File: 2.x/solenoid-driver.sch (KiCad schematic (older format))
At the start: 69 parts, among them P3 CONN_8X2, Q1 BC846, Q10 BC846, Q11 BC846, Q12 BC846, Q2 BC846, Q3 BC846, Q4 BC846, Q5 DMN6040SSD, Q6 DMN6040SSD, Q7 DMN6040SSD, Q8 DMN6040SSD, Q9 BC846

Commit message: Cleaning up schematic Updating solenoid driver to use 12V for MOSFET gates instead of Vsol so we never exceed Vgs_max
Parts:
- R11, R13, R15, R33, R35, R37, R39, R9: value 18K -> 1K
- R21, R22, R23, R24, R25, R26, R27, R28: value 27K -> 4.7K
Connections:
- net labels added: SOL_12V
- wire segments 244 -> 245
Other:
- moved on the sheet: D1, D2, D3, D4, D5, D6, D7, D8, Q1, Q10, Q11, Q12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

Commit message: Started layout on 2.0
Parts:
- removed P3: CONN_8X2, symbol CONN_8X2
- added D39, D40, D41, D42, D43, D44, D45, D46: S1M, Diodes_SMD:Diode-SMA_Standard, symbol DIODE
- added P3: SOLENOID-CONNECTOR, PinballParts:SOLENOID-CONNECTOR-V, symbol SOLENOID-CONNECTOR
- D1, D8: footprint ~ -> LEDs:LED-0603
- D2: renamed from D5; footprint ~ -> LEDs:LED-0603
- D3: renamed from D2; footprint ~ -> LEDs:LED-0603
- D4: renamed from D6; footprint ~ -> LEDs:LED-0603
- D5: renamed from D3; footprint ~ -> LEDs:LED-0603
- D6: renamed from D7; footprint ~ -> LEDs:LED-0603
- D7: renamed from D4; footprint ~ -> LEDs:LED-0603
- Q1, Q12: footprint SOT-23 -> Housings_SOT-23_SOT-143_TSOT-6:SOT-23
- Q10: renamed from Q8; footprint SO8 -> Housings_SOIC:SOIC-8_3.9x4.9mm_Pitch1.27mm
- Q11: renamed from Q4; footprint SOT-23 -> Housings_SOT-23_SOT-143_TSOT-6:SOT-23
- Q2: renamed from Q9; footprint SOT-23 -> Housings_SOT-23_SOT-143_TSOT-6:SOT-23
- Q3: renamed from Q5; footprint SO8 -> Housings_SOIC:SOIC-8_3.9x4.9mm_Pitch1.27mm
- Q4: renamed from Q7; footprint SO8 -> Housings_SOIC:SOIC-8_3.9x4.9mm_Pitch1.27mm
- Q5: renamed from Q2; footprint SOT-23 -> Housings_SOT-23_SOT-143_TSOT-6:SOT-23
- Q6: renamed from Q10; footprint SOT-23 -> Housings_SOT-23_SOT-143_TSOT-6:SOT-23
- Q7: renamed from Q3; footprint SOT-23 -> Housings_SOT-23_SOT-143_TSOT-6:SOT-23
- Q8: renamed from Q11; footprint SOT-23 -> Housings_SOT-23_SOT-143_TSOT-6:SOT-23
- Q9: renamed from Q6; footprint SO8 -> Housings_SOIC:SOIC-8_3.9x4.9mm_Pitch1.27mm
- R1: renamed from R5; footprint ~ -> Resistors_SMD:R_0603
- R10: renamed from R45; footprint ~ -> Resistors_SMD:R_0603
- R11: renamed from R17; footprint ~ -> Resistors_SMD:R_0603
- R12: renamed from R29; footprint ~ -> Resistors_SMD:R_0603
- R13: renamed from R6; footprint ~ -> Resistors_SMD:R_0603
- R14: renamed from R11; footprint ~ -> Resistors_SMD:R_0603
- R15: renamed from R22; value 4.7K -> 2.7K; footprint ~ -> Resistors_SMD:R_0603
- R16: renamed from R26; value 4.7K -> 2.7K; footprint ~ -> Resistors_SMD:R_0603
- R17: renamed from R35; footprint ~ -> Resistors_SMD:R_0603
- R18: renamed from R42; footprint ~ -> Resistors_SMD:R_0603
- R19: renamed from R2; footprint ~ -> Resistors_SMD:R_0603
- R2: renamed from R9; footprint ~ -> Resistors_SMD:R_0603
- R20: renamed from R12; footprint ~ -> Resistors_SMD:R_0603
- R21: renamed from R36; footprint ~ -> Resistors_SMD:R_0603
- R22: renamed from R46; footprint ~ -> Resistors_SMD:R_0603
- R23: renamed from R18; footprint ~ -> Resistors_SMD:R_0603
- R24: renamed from R30; footprint ~ -> Resistors_SMD:R_0603
- R25: renamed from R7; footprint ~ -> Resistors_SMD:R_0603
- R26: renamed from R13; footprint ~ -> Resistors_SMD:R_0603
- R27: renamed from R23; value 4.7K -> 2.7K; footprint ~ -> Resistors_SMD:R_0603
- R28: renamed from R27; value 4.7K -> 2.7K; footprint ~ -> Resistors_SMD:R_0603
- R29: renamed from R37; footprint ~ -> Resistors_SMD:R_0603
- R3: renamed from R21; value 4.7K -> 2.7K; footprint ~ -> Resistors_SMD:R_0603
- R30: renamed from R43; footprint ~ -> Resistors_SMD:R_0603
- R31: renamed from R3; footprint ~ -> Resistors_SMD:R_0603
- R32: renamed from R14; footprint ~ -> Resistors_SMD:R_0603
- R33: renamed from R38; footprint ~ -> Resistors_SMD:R_0603
- R34: renamed from R47; footprint ~ -> Resistors_SMD:R_0603
- R35: renamed from R19; footprint ~ -> Resistors_SMD:R_0603
- R36: renamed from R31; footprint ~ -> Resistors_SMD:R_0603
- R37: renamed from R8; footprint ~ -> Resistors_SMD:R_0603
- R38: renamed from R15; footprint ~ -> Resistors_SMD:R_0603
- R39: renamed from R24; value 4.7K -> 2.7K; footprint ~ -> Resistors_SMD:R_0603
- R4: renamed from R25; value 4.7K -> 2.7K; footprint ~ -> Resistors_SMD:R_0603
- R40: renamed from R28; value 4.7K -> 2.7K; footprint ~ -> Resistors_SMD:R_0603
- R41: renamed from R39; footprint ~ -> Resistors_SMD:R_0603
- R42: renamed from R44; footprint ~ -> Resistors_SMD:R_0603
- R43: renamed from R4; footprint ~ -> Resistors_SMD:R_0603
- R44: renamed from R16; footprint ~ -> Resistors_SMD:R_0603
- R45: renamed from R40; footprint ~ -> Resistors_SMD:R_0603
- R46: renamed from R48; footprint ~ -> Resistors_SMD:R_0603
- R47: renamed from R20; footprint ~ -> Resistors_SMD:R_0603
- R48: renamed from R32; footprint ~ -> Resistors_SMD:R_0603
- R5: renamed from R33; footprint ~ -> Resistors_SMD:R_0603
- R6: renamed from R41; footprint ~ -> Resistors_SMD:R_0603
- R7: renamed from R1; footprint ~ -> Resistors_SMD:R_0603
- R8: renamed from R10; footprint ~ -> Resistors_SMD:R_0603
- R9: renamed from R34; footprint ~ -> Resistors_SMD:R_0603
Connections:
- wire segments 245 -> 271
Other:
- moved on the sheet: D1, D2, D3, D4, D5, D6, D7, D8, Q1, Q10A, Q10B, Q11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

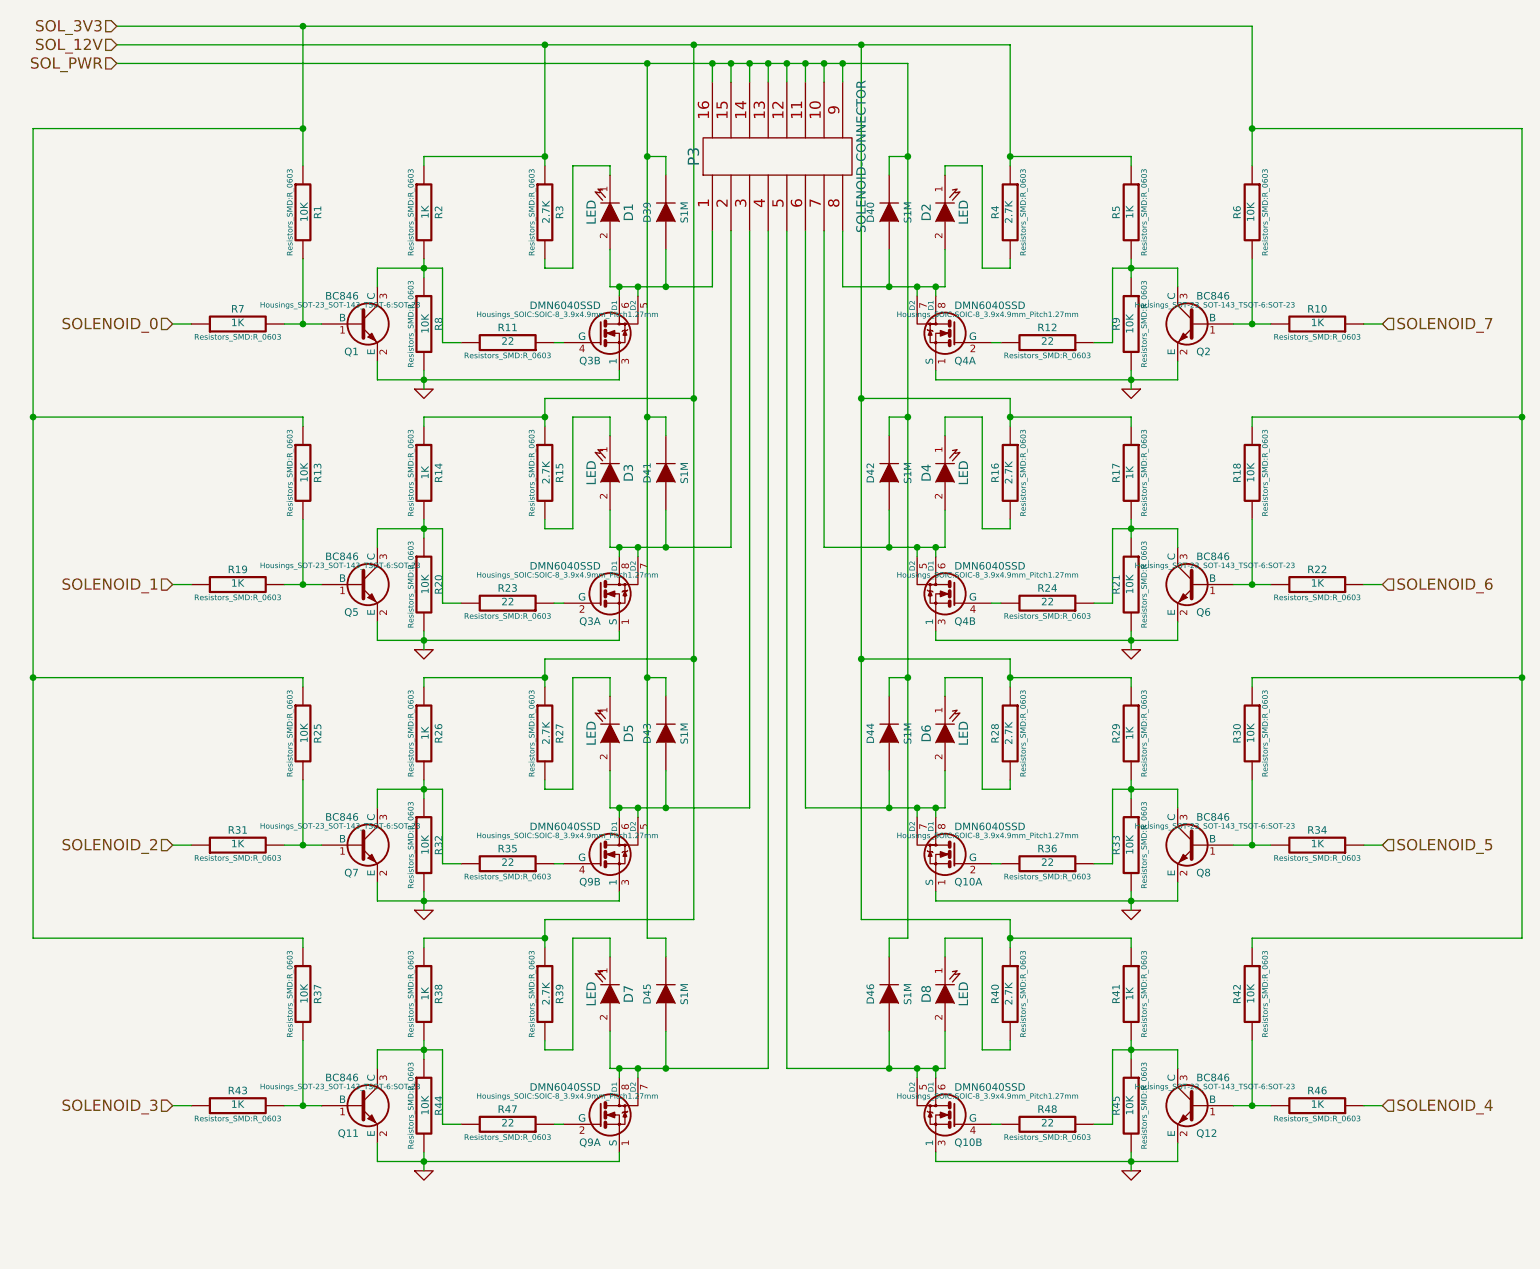
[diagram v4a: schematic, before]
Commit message: Updated solenoid driver with new resistor arrangement, and changed footprint on switch matrix to a connector we can actually get.
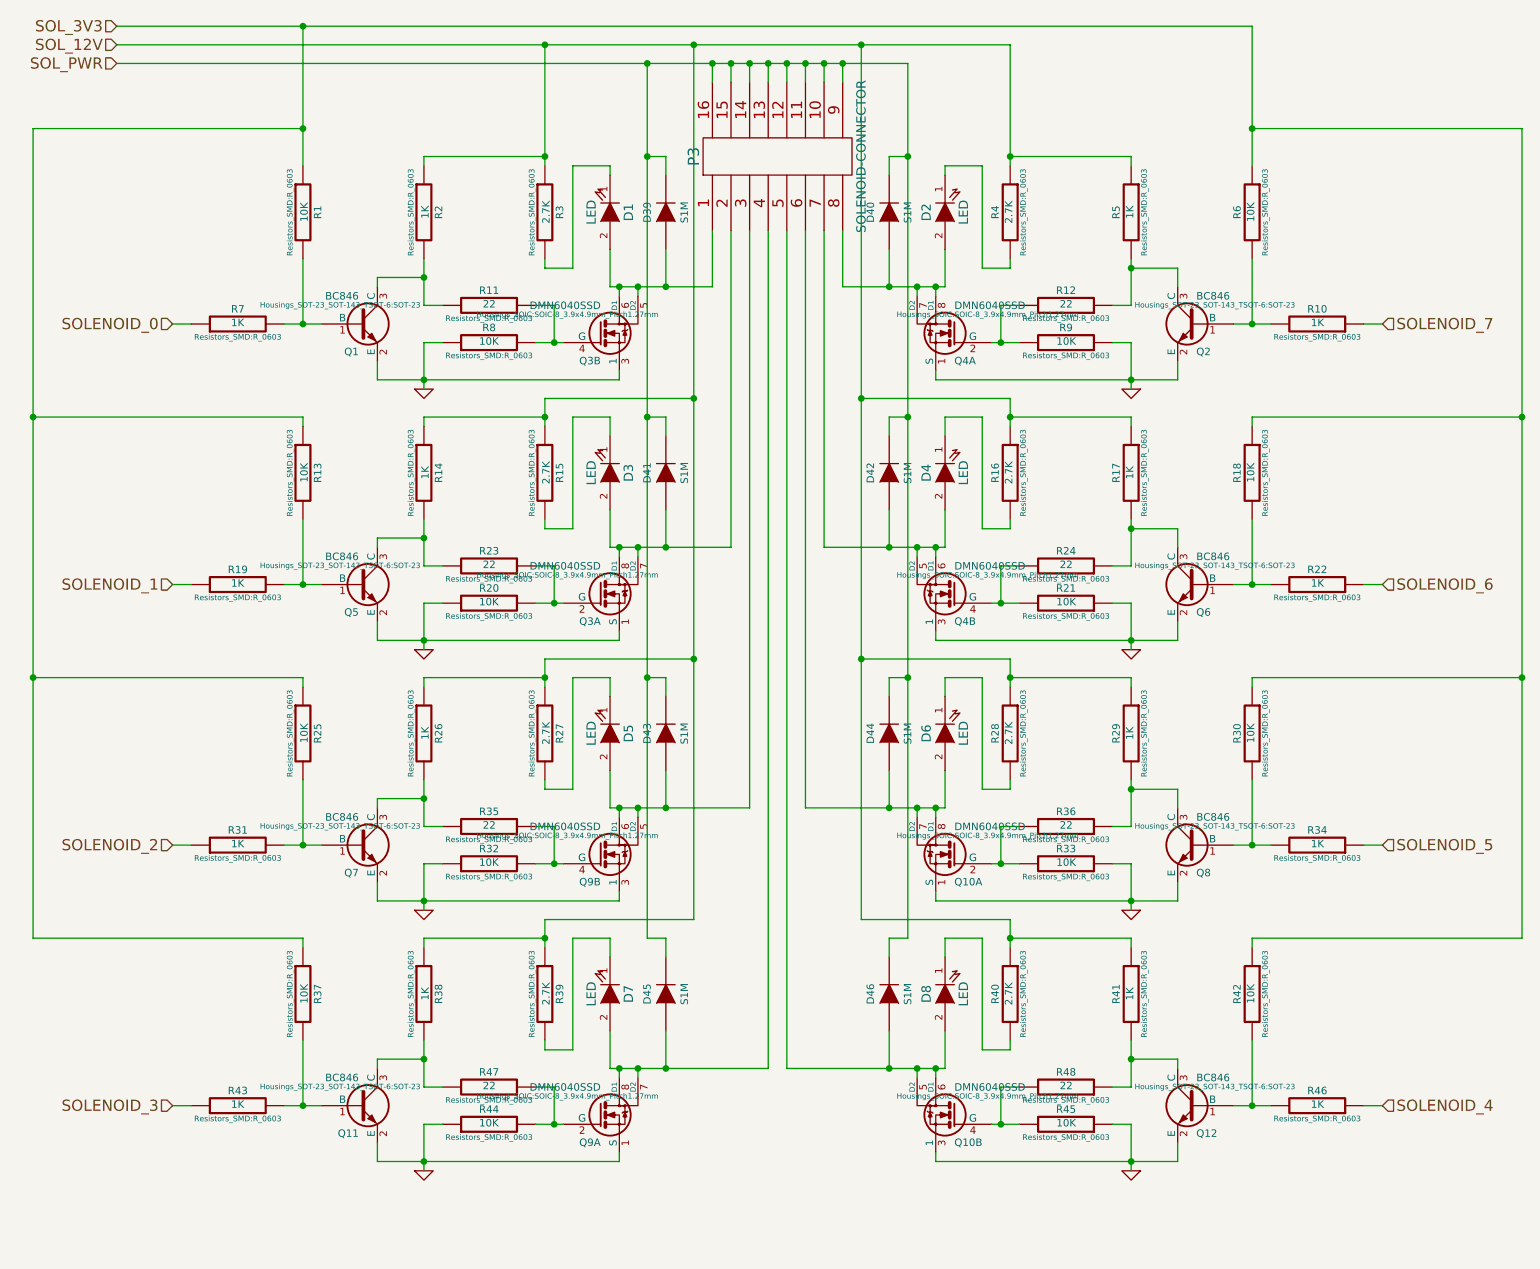
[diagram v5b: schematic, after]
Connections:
- net GND: now also R20.1, R21.1, R32.1, R33.1, R44.1, R45.1, R8.1, R9.1; no longer R20.2, R21.2, R32.2, R33.2, R44.2, R45.2, R8.2, R9.2
- net at Q1.3 (C), R11.2, R2.2: no longer R8.1
- net at Q5.3 (C), R14.2, R23.2: no longer R20.1
- net at Q7.3 (C), R26.2, R35.2: no longer R32.1
- net at Q11.3 (C), R38.2, R47.2: no longer R44.1
- net at Q2.3 (C), R12.1, R5.2: no longer R9.1
- net at Q6.3 (C), R17.2, R24.1: no longer R21.1
- net at Q8.3 (C), R29.2, R36.1: no longer R33.1
- net at Q12.3 (C), R41.2, R48.1: no longer R45.1
- net at Q3.4 (G), R11.1: now also R8.2
- net at Q4.2 (G), R12.2: now also R9.2
- net at Q3.2 (G), R23.1: now also R20.2
- net at Q9.4 (G), R35.1: now also R32.2
- net at Q9.2 (G), R47.1: now also R44.2
- net at Q4.4 (G), R24.2: now also R21.2
- net at Q10.2 (G), R36.2: now also R33.2
- net at Q10.4 (G), R48.2: now also R45.2
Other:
- moved on the sheet: R11, R12, R20, R21, R23, R24, R32, R33, R35, R36, R44, R45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

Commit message: Committing latest files. This includes the KiCAD 4.0.0rc1 migration as well as the updates to Base Board 2.1.
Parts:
- removed D39, D40, D41, D42, D43, D44, D45, D46: S1M, Diodes_SMD:Diode-SMA_Standard, symbol DIODE
- added D39, D40, D41, D42, D43, D44, D45, D46: S1M, Diodes_SMD:SMA_Standard, symbol D
- R1, R10, R11, R12, R13, R14, R15, R16, R17, R18, R19, R2, R20, R21, R22, R23, R24, R25, R26, R27, R28, R29, R3, R30, R31, R32, R33, R34, R35, R36, R37, R38, R39, R4, R40, R41, R42, R43, R44, R45, R46, R47, R48, R5, R6, R7, R8, R9: symbol R -> R-RESCUE-base-module-hardware-v2
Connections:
- net SOL_PWR: now also D39.1 (K), D40.1 (K), D41.1 (K), D42.1 (K), D43.1 (K), D44.1 (K), D45.1 (K), D46.1 (K)
- net at R3.2: now also D1.2 (A); no longer D1.1 (K)
- net at P3.1, Q3.5 (D2), Q3.6 (D1): now also D1.1 (K), D39.2 (A); no longer D1.2 (A)
- net at R15.2: now also D3.2 (A); no longer D3.1 (K)
- net at P3.2, Q3.7 (D2), Q3.8 (D1): now also D3.1 (K), D41.2 (A); no longer D3.2 (A)
- net at R27.2: now also D5.2 (A); no longer D5.1 (K)
- net at P3.3, Q9.5 (D2), Q9.6 (D1): now also D5.1 (K), D43.2 (A); no longer D5.2 (A)
- net at R39.2: now also D7.2 (A); no longer D7.1 (K)
- net at P3.4, Q9.7 (D2), Q9.8 (D1): now also D7.1 (K), D45.2 (A); no longer D7.2 (A)
- net at R4.2: now also D2.2 (A); no longer D2.1 (K)
- net at P3.8, Q4.7 (D2), Q4.8 (D1): now also D2.1 (K), D40.2 (A); no longer D2.2 (A)
- net at R16.2: now also D4.2 (A); no longer D4.1 (K)
- net at P3.7, Q4.5 (D2), Q4.6 (D1): now also D4.1 (K), D42.2 (A); no longer D4.2 (A)
- net at R28.2: now also D6.2 (A); no longer D6.1 (K)
- net at P3.6, Q10.7 (D2), Q10.8 (D1): now also D6.1 (K), D44.2 (A); no longer D6.2 (A)
- net at R40.2: now also D8.2 (A); no longer D8.1 (K)
- net at P3.5, Q10.5 (D2), Q10.6 (D1): now also D8.1 (K), D46.2 (A); no longer D8.2 (A)
